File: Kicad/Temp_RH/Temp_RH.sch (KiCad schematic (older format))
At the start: 8 parts, among them J1 DHT 11, J2 Arduino, J3 DHT 22, J4 SHT 75, J5 SHT 31

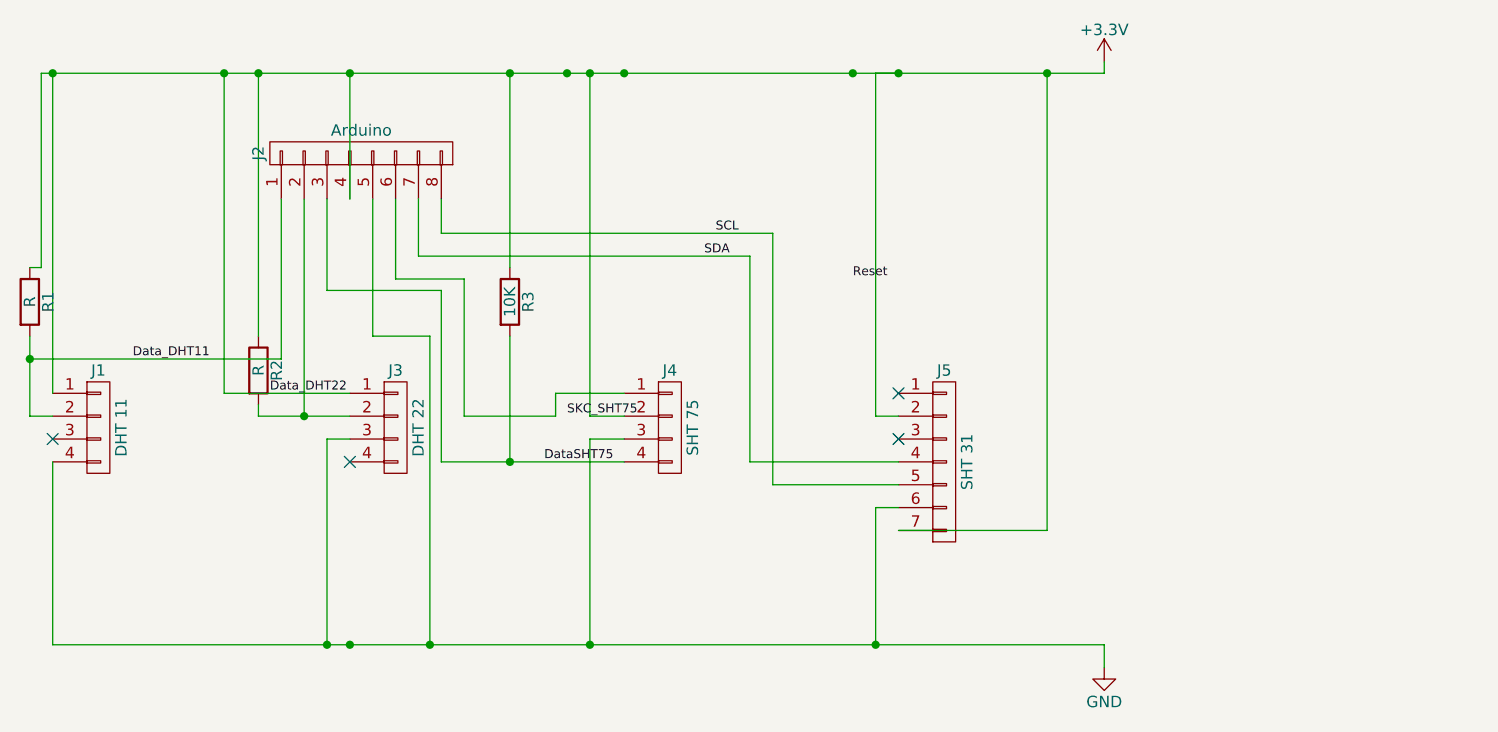
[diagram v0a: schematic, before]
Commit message: Added PCB project for T&RH sensors by AndreBotCardoso. Moved Gas sensor's PCB projec directory. Added Main_board PCB project.
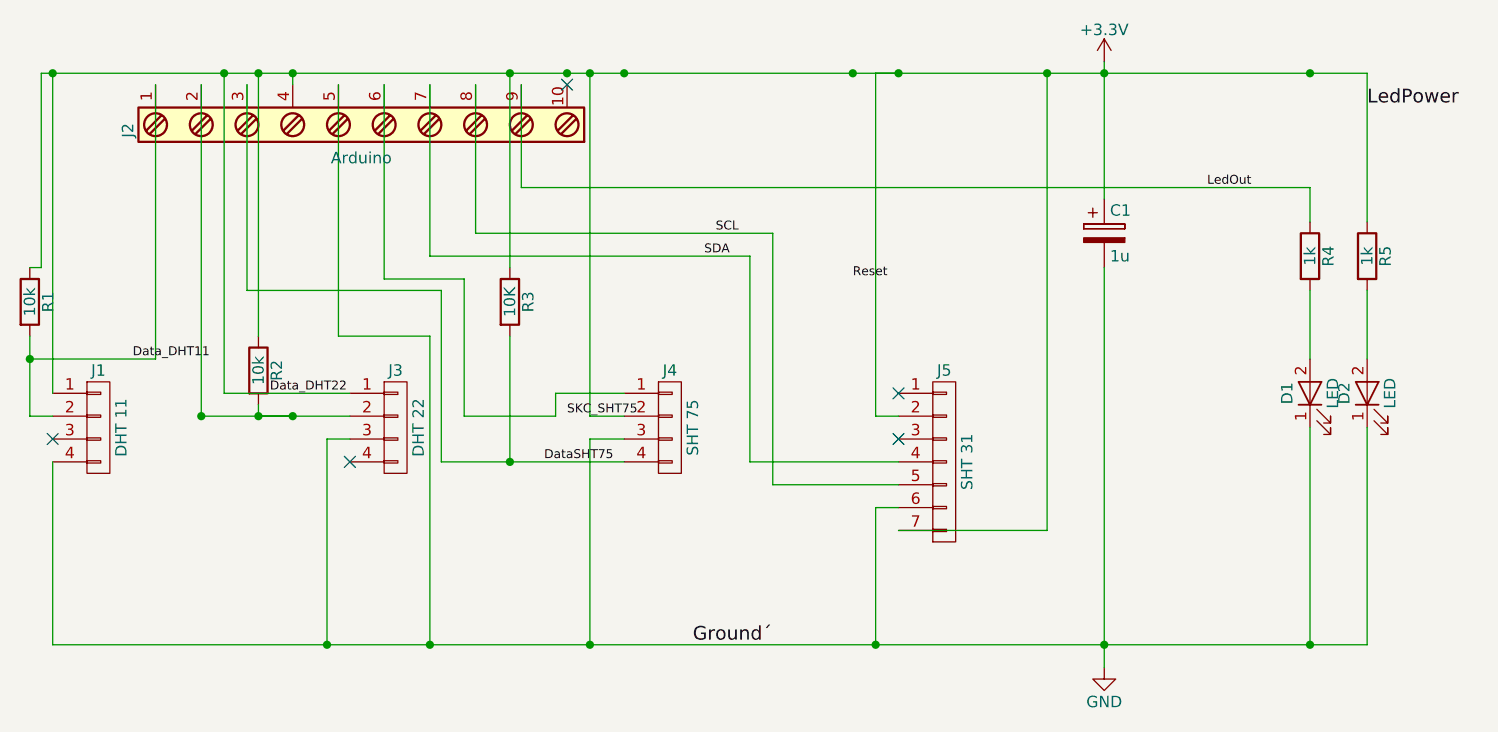
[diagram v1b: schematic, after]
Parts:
- removed J2: Arduino, Pin_Headers:Pin_Header_Straight_1x08_Pitch1.27mm, symbol CONN_01X08
- added C1: 1u, Capacitors_THT:CP_Radial_D4.0mm_P1.50mm, symbol CP
- added D1, D2: LED, LEDs:LED_D1.8mm_W3.3mm_H2.4mm, symbol LED
- added J2: Arduino, Connectors_Terminal_Blocks:TerminalBlock_Pheonix_MPT-2.54mm_10pol, symbol Screw_Terminal_1x10
- added R4, R5: 1k, Resistors_THT:R_Axial_DIN0204_L3.6mm_D1.6mm_P5.08mm_Horizontal, symbol R
- R1, R2: value R -> 10k; footprint Resistors_THT:R_Axial_DIN0204_L3.6mm_D1.6mm_P7.62mm_Horizontal -> Resistors_THT:R_Axial_DIN0204_L3.6mm_D1.6mm_P5.08mm_Horizontal
- R3: footprint Resistors_THT:R_Axial_DIN0204_L3.6mm_D1.6mm_P7.62mm_Horizontal -> Resistors_THT:R_Axial_DIN0204_L3.6mm_D1.6mm_P5.08mm_Horizontal
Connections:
- net +3V3: now also C1.1, J2.4, R5.1
- net DataSHT75: now also J2.3
- net Data_DHT11: now also J2.1
- net GND: now also C1.2, D1.1 (K), D2.1 (K), J2.5
- net SCL: now also J2.8
- net SDA: now also J2.7
- net at J3.2 (P2), R2.2: now also J2.2
- net at J4.1 (P1): now also J2.6
- new net: D1.2 (A), R4.2
- new net: D2.2 (A), R5.2
- new net LedOut: J2.9, R4.1
- no-connect marks 4 -> 5
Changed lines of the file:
@@
 LIBS:contrib
 LIBS:valves
+LIBS:Temp_RH-cache
 EELAYER 25 0
 EELAYER END
@@
 F 0 "R3" V 3930 1650 50  0000 C CNN
 F 1 "10K" V 3850 1650 50  0000 C CNN
-F 2 "Resistors_THT:R_Axial_DIN0204_L3.6mm_D1.6mm_P7.62mm_Horizontal" V 3780 1650 50  0001 C CNN
+F 2 "Resistors_THT:R_Axial_DIN0204_L3.6mm_D1.6mm_P5.08mm_Horizontal" V 3780 1650 50  0001 C CNN
 F 3 "" H 3850 1650 50  0001 C CNN
 	1    3850 1650
@@
 Text Label 4700 1450 0    39   ~ 0
 SDA
+$Comp
+L R R1
+U 1 1 5963B018
+P 1750 1650
+F 0 "R1" V 1830 1650 50  0000 C CNN
+F 1 "10k" V 1750 1650 50  0000 C CNN
+F 2 "Resistors_THT:R_Axial_DIN0204_L3.6mm_D1.6mm_P5.08mm_Horizontal" V 1680 1650 50  0001 C CNN
+F 3 "" H 1750 1650 50  0001 C CNN
+	1    1750 1650
+	1    0    0    -1
+$EndComp
+$Comp
+L R R2
+U 1 1 5963B4BA
+P 2750 1950
+F 0 "R2" V 2830 1950 50  0000 C CNN
+F 1 "10k" V 2750 1950 50  0000 C CNN
+F 2 "Resistors_THT:R_Axial_DIN0204_L3.6mm_D1.6mm_P5.08mm_Horizontal" V 2680 1950 50  0001 C CNN
+F 3 "" H 2750 1950 50  0001 C CNN
+	1    2750 1950
+	1    0    0    -1
+$EndComp
+NoConn ~ 5550 2250
+NoConn ~ 5550 2050
+NoConn ~ 3150 2350
+NoConn ~ 1850 2250
+$Comp
+L CP C1
+U 1 1 59665A74
+P 6450 1350
+F 0 "C1" H 6475 1450 50  0000 L CNN
+F 1 "1u" H 6475 1250 50  0000 L CNN
+F 2 "Capacitors_THT:CP_Radial_D4.0mm_P1.50mm" H 6488 1200 50  0001 C CNN
+F 3 "" H 6450 1350 50  0001 C CNN
+	1    6450 1350
+	1    0    0    -1
+$EndComp
+$Comp
+L R R4
+U 1 1 596664A3
+P 7350 1450
+F 0 "R4" V 7430 1450 50  0000 C CNN
+F 1 "1k" V 7350 1450 50  0000 C CNN
+F 2 "Resistors_THT:R_Axial_DIN0204_L3.6mm_D1.6mm_P5.08mm_Horizontal" V 7280 1450 50  0001 C CNN
+F 3 "" H 7350 1450 50  0001 C CNN
+	1    7350 1450
+	1    0    0    -1
+$EndComp
+$Comp
+L R R5
+U 1 1 59666750
+P 7600 1450
+F 0 "R5" V 7680 1450 50  0000 C CNN
+F 1 "1k" V 7600 1450 50  0000 C CNN
+F 2 "Resistors_THT:R_Axial_DIN0204_L3.6mm_D1.6mm_P5.08mm_Horizontal" V 7530 1450 50  0001 C CNN
+F 3 "" H 7600 1450 50  0001 C CNN
+	1    7600 1450
+	1    0    0    -1
+$EndComp
+$Comp
+L LED D1
+U 1 1 596667D0
+P 7350 2050
+F 0 "D1" H 7350 2150 50  0000 C CNN
+F 1 "LED" H 7350 1950 50  0000 C CNN
+F 2 "LEDs:LED_D1.8mm_W3.3mm_H2.4mm" H 7350 2050 50  0001 C CNN
+F 3 "" H 7350 2050 50  0001 C CNN
+	1    7350 2050
+	0    -1   -1   0
+$EndComp
+Text Label 7600 800  0    60   ~ 0
+LedPower
 Wire Wire Line
 	3850 1800 3850 2350
@@
 	2600 2050 2600 650
 Wire Wire Line
-	2750 2150 3150 2150
+	2500 2150 3150 2150
 Wire Wire Line
 	1750 2150 1850 2150
@@
 	4900 2350 4900 1450
 Wire Wire Line
-	6450 650  6450 600
-Wire Wire Line
-	6450 3150 6450 3250
-Wire Wire Line
-	1850 3150 6450 3150
-Connection ~ 3150 3150
+	6450 600  6450 1200
+Wire Wire Line
+	6450 1500 6450 3250
 Connection ~ 5450 3150
 Wire Wire Line
-	1800 650  6450 650
+	1800 650  7600 650
 Connection ~ 5550 650
 Connection ~ 5350 650
 Connection ~ 3850 650
 Connection ~ 2600 650
-$Comp
-L R R1
-U 1 1 5963B018
-P 1750 1650
-F 0 "R1" V 1830 1650 50  0000 C CNN
-F 1 "R" V 1750 1650 50  0000 C CNN
-F 2 "Resistors_THT:R_Axial_DIN0204_L3.6mm_D1.6mm_P7.62mm_Horizontal" V 1680 1650 50  0001 C CNN
-F 3 "" H 1750 1650 50  0001 C CNN
-	1    1750 1650
-	1    0    0    -1
-$EndComp
-$Comp
-L R R2
-U 1 1 5963B4BA
-P 2750 1950
-F 0 "R2" V 2830 1950 50  0000 C CNN
-F 1 "R" V 2750 1950 50  0000 C CNN
-F 2 "Resistors_THT:R_Axial_DIN0204_L3.6mm_D1.6mm_P7.62mm_Horizontal" V 2680 1950 50  0001 C CNN
-F 3 "" H 2750 1950 50  0001 C CNN
-	1    2750 1950
-	1    0    0    -1
-$EndComp
 Wire Wire Line
 	3150 2250 3050 2250
@@
 Wire Wire Line
 	1750 1500 1800 1500
-$Comp
-L CONN_01X08 J2
-U 1 1 5963BC06
-P 3200 1000
-F 0 "J2" H 3200 1450 50  0000 C CNN
-F 1 "Arduino" V 3300 1000 50  0000 C CNN
-F 2 "Pin_Headers:Pin_Header_Straight_1x08_Pitch1.27mm" H 3200 1000 50  0001 C CNN
-F 3 "" H 3200 1000 50  0001 C CNN
-	1    3200 1000
-	0    -1   -1   0
-$EndComp
-Wire Wire Line
-	3550 1350 3550 1200
-Wire Wire Line
-	5000 1350 3550 1350
-Wire Wire Line
-	3450 1200 3450 1450
-Wire Wire Line
-	2850 1200 2850 1900
-Wire Wire Line
-	2950 1200 2950 2150
-Wire Wire Line
-	2850 1900 1750 1900
-Connection ~ 2950 2150
-Wire Wire Line
-	3450 1450 4900 1450
-Wire Wire Line
-	3650 1550 3350 1550
-Wire Wire Line
-	3350 1550 3350 1200
-Wire Wire Line
-	3550 1600 3050 1600
-Wire Wire Line
-	3050 1600 3050 1200
-Wire Wire Line
-	3150 1200 3150 650
-Connection ~ 3150 650
-Wire Wire Line
-	3250 1200 3250 1800
-Wire Wire Line
-	3250 1800 3500 1800
+Wire Wire Line
+	3700 1350 3700 700
+Wire Wire Line
+	5000 1350 3700 1350
+Wire Wire Line
+	3500 700  3500 1450
+Wire Wire Line
+	2300 700  2300 1900
+Wire Wire Line
+	2500 700  2500 2150
+Wire Wire Line
+	2300 1900 1750 1900
+Connection ~ 2500 2150
+Wire Wire Line
+	3500 1450 4900 1450
+Wire Wire Line
+	3650 1550 3300 1550
+Wire Wire Line
+	3300 1550 3300 700
+Wire Wire Line
+	3550 1600 2700 1600
+Wire Wire Line
+	2700 1600 2700 700
+Wire Wire Line
+	2900 700  2900 650
+Connection ~ 2900 650
+Wire Wire Line
+	3100 700  3100 1800
+Wire Wire Line
+	3100 1800 3500 1800
 Wire Wire Line
 	3500 1800 3500 3150
@@
 Wire Wire Line
 	5550 2350 4900 2350
-NoConn ~ 5550 2250
-NoConn ~ 5550 2050
-NoConn ~ 3150 2350
-NoConn ~ 1850 2250
 Wire Wire Line
 	5450 2150 5450 650
 Wire Wire Line
 	5450 650  5550 650
+Connection ~ 6450 650
+Connection ~ 6450 3150
+Wire Wire Line
+	7600 650  7600 1300
+Connection ~ 7350 650
+Wire Wire Line
+	7350 1300 7350 1150
+Wire Wire Line
+	7600 1600 7600 1900
+$Comp
+L Screw_Terminal_1x10 J2
+U 1 1 59668A2D
+P 3200 900
+F 0 "J2" H 3200 1950 50  0000 C TNN
+F 1 "Arduino" V 3050 900 50  0000 C TNN
+F 2 "Connectors_Terminal_Blocks:TerminalBlock_Pheonix_MPT-2.54mm_10pol" H 3200 -125 50  0001 C CNN
+F 3 "" H 3175 1700 50  0001 C CNN
+	1    3200 900
+	0    -1   -1   0
+$EndComp
+Wire Wire Line
+	7350 1150 3900 1150
+Wire Wire Line
+	3900 1150 3900 700
+Text Label 6900 1150 0    39   ~ 0
+LedOut
+$Comp
+L LED D2
+U 1 1 5966685B
+P 7600 2050
+F 0 "D2" H 7600 2150 50  0000 C CNN
+F 1 "LED" H 7600 1950 50  0000 C CNN
+F 2 "LEDs:LED_D1.8mm_W3.3mm_H2.4mm" H 7600 2050 50  0001 C CNN
+F 3 "" H 7600 2050 50  0001 C CNN
+	1    7600 2050
+	0    -1   -1   0
+$EndComp
+Wire Wire Line
+	7350 1600 7350 1900
+Wire Wire Line
+	7350 3150 7350 2200
+Wire Wire Line
+	7600 3150 7600 2200
+Connection ~ 7350 3150
+NoConn ~ 4100 700
+Text Label 4650 3150 0    60   ~ 0
+Ground´
+Wire Wire Line
+	2900 2150 2750 2150
+Connection ~ 2750 2150
+Connection ~ 2900 2150
+Wire Wire Line
+	1850 3150 7600 3150
 $EndSCHEMATC

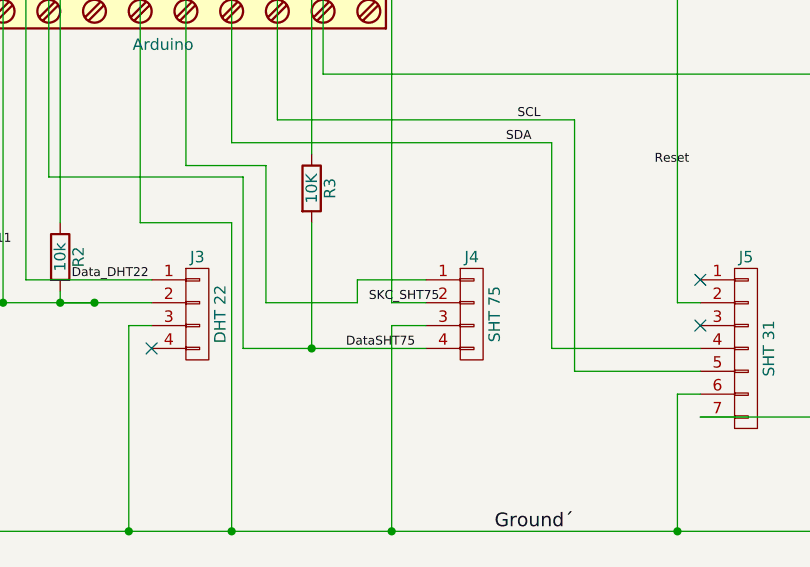
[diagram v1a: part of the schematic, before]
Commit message: Added RTC. RTC integration with SD file paths and log files. Added time tag to data log.
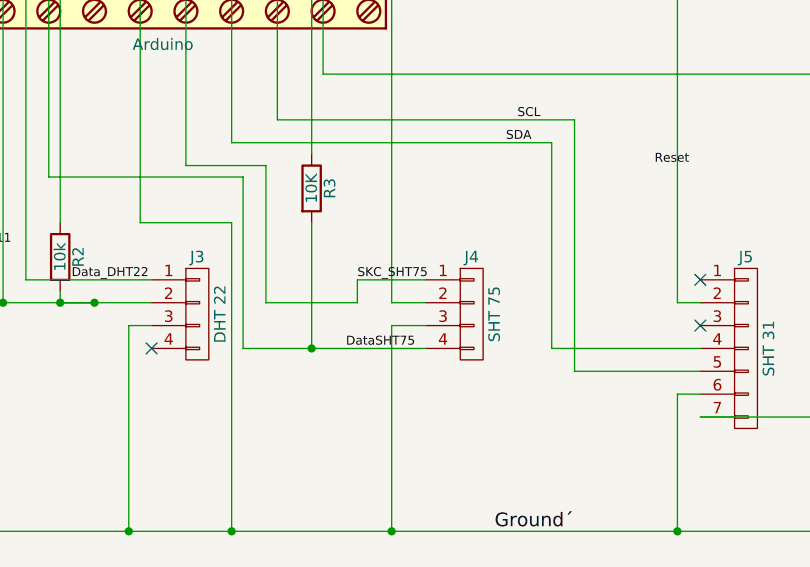
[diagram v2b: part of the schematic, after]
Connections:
- net SKC_SHT75: now also J2.6, J4.1 (P1)
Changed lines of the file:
@@
 Text Label 4000 2350 0    39   ~ 0
 DataSHT75
-Text Label 4100 2150 0    39   ~ 0
+Text Label 4050 2050 0    39   ~ 0
 SKC_SHT75
 Text Label 2800 2050 0    39   ~ 0

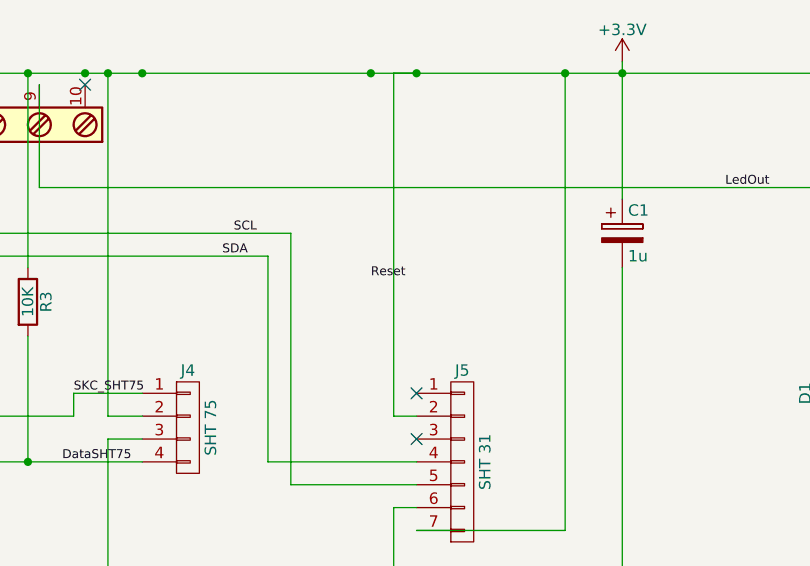
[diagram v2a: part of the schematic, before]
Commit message: Temperature and Temperature+RH (TTRH) sensors are all implemented. All sensors were tested, except Thermopar temperature sensor. Added TTRH shield schematic and layout (missing SDA1 and SCL1 for SHT75).
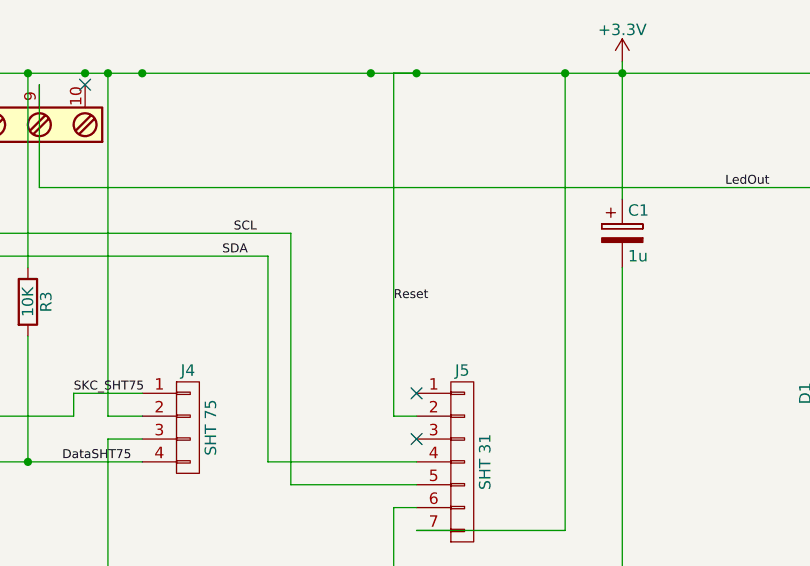
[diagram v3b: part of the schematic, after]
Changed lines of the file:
@@
 	1    0    0    -1
 $EndComp
-Text Label 5350 1550 0    39   ~ 0
+Text Label 5450 1650 0    39   ~ 0
 Reset
 Text Label 4750 1350 0    39   ~ 0
